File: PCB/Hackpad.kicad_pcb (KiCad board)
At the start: 2 copper layers, 70.1 x 46 mm, 7 parts, among them SW1 SW_Push, SW2 SW_Push, SW3 SW_Push, SW4 SW_Push, U1 XIAO-RP2040-DIP

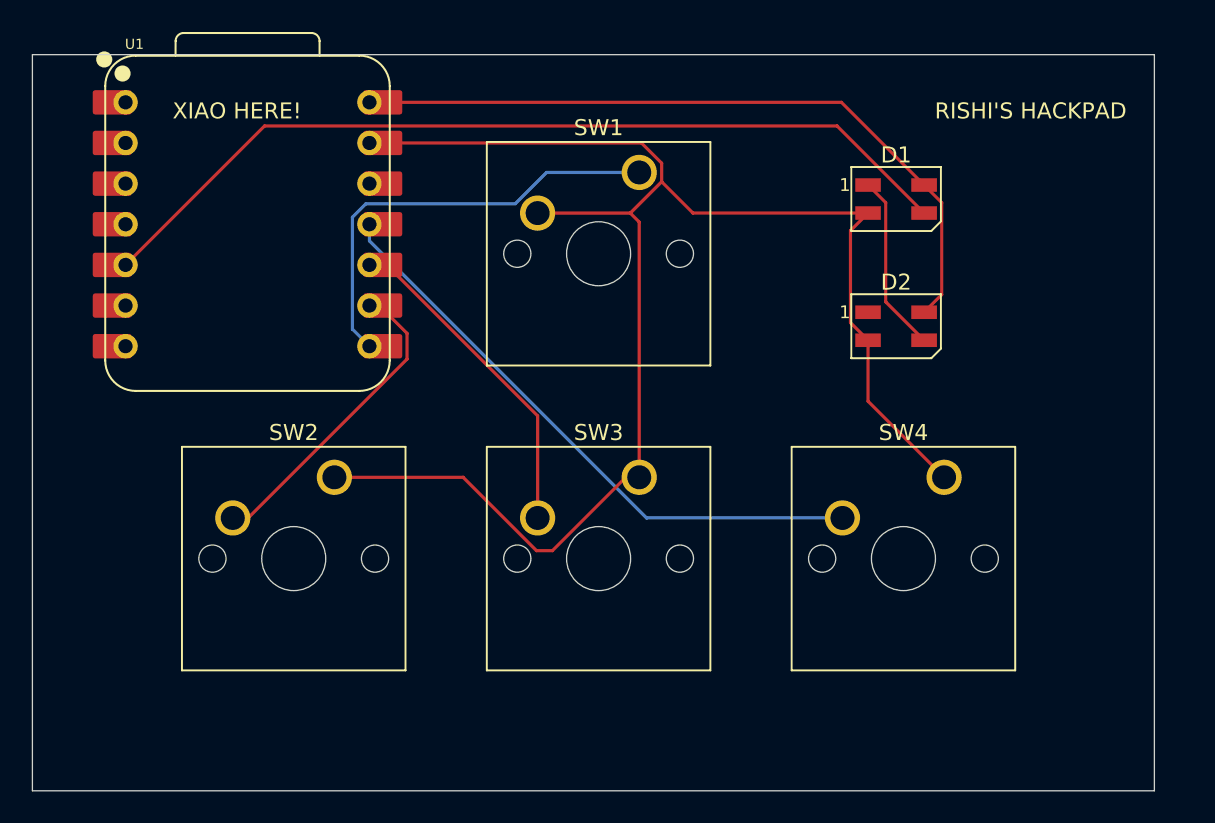
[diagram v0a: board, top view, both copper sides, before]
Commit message: fixed kicad files
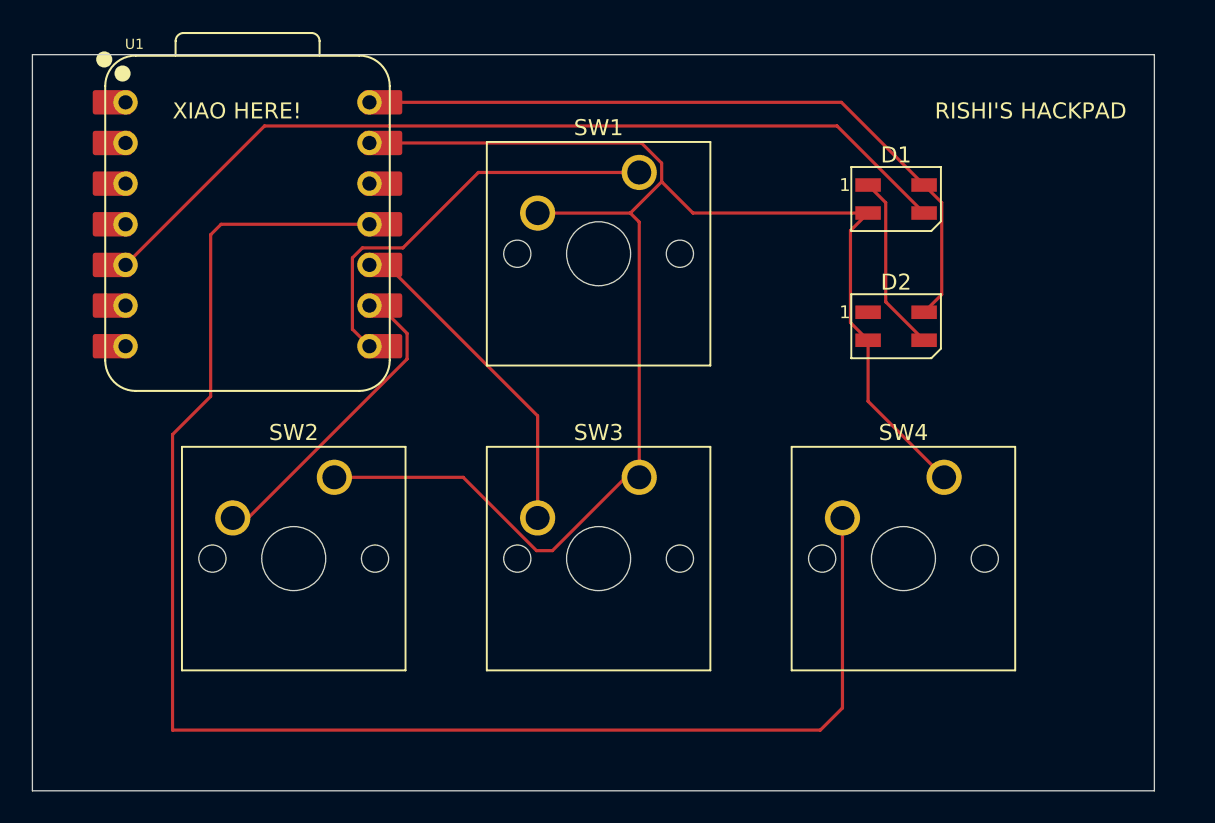
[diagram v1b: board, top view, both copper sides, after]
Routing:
- net Net-(U1-GPIO3/MOSI): track 37.8 -> 96.4 mm
- net Net-(U1-GPIO1/RX): track 27.6 -> 27.0 mm
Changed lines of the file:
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@@
 			(outputformat 1)
 			(mirror no)
-			(drillshape 1)
+			(drillshape 0)
 			(scaleselection 1)
-			(outputdirectory "")
+			(outputdirectory "./")
 		)
 	)
@@
 	(segment
 		(start 139.827 101.1555)
-		(end 139.827 94.15819)
-		(width 0.2)
-		(layer "B.Cu")
+		(end 140.89 102.2185)
+		(width 0.2)
+		(layer "F.Cu")
 		(net 3)
 	)
 	(segment
-		(start 149.999 93.319686)
-		(end 151.958686 91.36)
-		(width 0.2)
-		(layer "B.Cu")
+		(start 147.696126 91.36)
+		(end 142.980626 96.0755)
+		(width 0.2)
+		(layer "F.Cu")
 		(net 3)
 	)
 	(segment
-		(start 139.827 94.15819)
-		(end 140.665504 93.319686)
-		(width 0.2)
-		(layer "B.Cu")
+		(start 157.75 91.36)
+		(end 157.75 92.28125)
+		(width 0.2)
+		(layer "F.Cu")
 		(net 3)
 	)
 	(segment
-		(start 140.89 102.2185)
+		(start 142.980626 96.0755)
+		(end 140.44969 96.0755)
+		(width 0.2)
+		(layer "F.Cu")
+		(net 3)
+	)
+	(segment
+		(start 140.44969 96.0755)
+		(end 139.827 96.69819)
+		(width 0.2)
+		(layer "F.Cu")
+		(net 3)
+	)
+	(segment
+		(start 157.75 91.36)
+		(end 147.696126 91.36)
+		(width 0.2)
+		(layer "F.Cu")
+		(net 3)
+	)
+	(segment
+		(start 139.827 96.69819)
 		(end 139.827 101.1555)
 		(width 0.2)
-		(layer "B.Cu")
-		(net 3)
-	)
-	(segment
-		(start 140.665504 93.319686)
-		(end 149.999 93.319686)
-		(width 0.2)
-		(layer "B.Cu")
-		(net 3)
-	)
-	(segment
-		(start 151.958686 91.36)
-		(end 157.75 91.36)
-		(width 0.2)
-		(layer "B.Cu")
+		(layer "F.Cu")
 		(net 3)
 	)
@@
 	)
 	(segment
-		(start 158.20481 112.95)
-		(end 140.89 95.63519)
-		(width 0.2)
-		(layer "B.Cu")
+		(start 140.89 94.5985)
+		(end 131.62025 94.5985)
+		(width 0.2)
+		(layer "F.Cu")
 		(net 6)
 	)
 	(segment
-		(start 140.89 95.63519)
-		(end 140.89 94.5985)
-		(width 0.2)
-		(layer "B.Cu")
+		(start 128.5875 126.20625)
+		(end 169.06875 126.20625)
+		(width 0.2)
+		(layer "F.Cu")
 		(net 6)
 	)
 	(segment
-		(start 170.45 112.95)
-		(end 158.20481 112.95)
-		(width 0.2)
-		(layer "B.Cu")
+		(start 128.5875 107.736)
+		(end 128.5875 126.20625)
+		(width 0.2)
+		(layer "F.Cu")
 		(net 6)
 	)
+	(segment
+		(start 130.96875 95.25)
+		(end 130.96875 105.35475)
+		(width 0.2)
+		(layer "F.Cu")
+		(net 6)
+	)
+	(segment
+		(start 170.45 124.825)
+		(end 170.45 112.95)
+		(width 0.2)
+		(layer "F.Cu")
+		(net 6)
+	)
+	(segment
+		(start 131.62025 94.5985)
+		(end 130.96875 95.25)
+		(width 0.2)
+		(layer "F.Cu")
+		(net 6)
+	)
+	(segment
+		(start 130.96875 105.35475)
+		(end 128.5875 107.736)
+		(width 0.2)
+		(layer "F.Cu")
+		(net 6)
+	)
+	(segment
+		(start 169.06875 126.20625)
+		(end 170.45 124.825)
+		(width 0.2)
+		(layer "F.Cu")
+		(net 6)
+	)
